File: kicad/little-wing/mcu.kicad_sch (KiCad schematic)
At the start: 30 parts, among them J8 Conn_ARM_SWD_TagConnect_TC203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, SW2 Reset, U1 ${ALTIUM_VALUE}, X1 ${ALTIUM_VALUE}, X2 ${ALTIUM_VALUE}

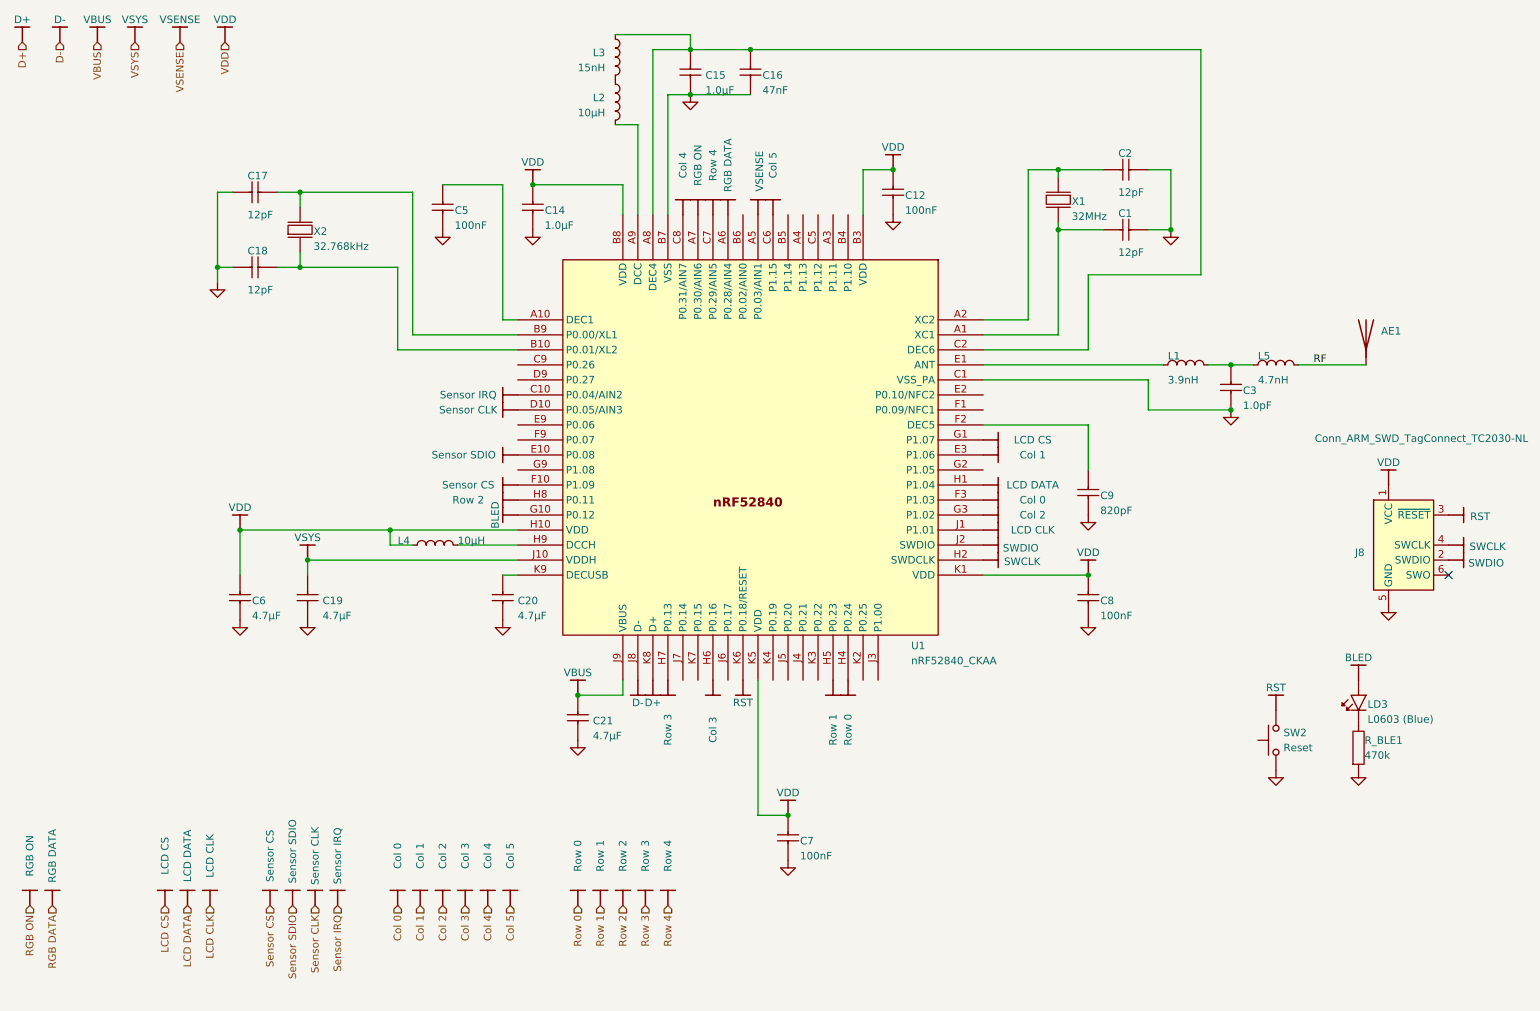
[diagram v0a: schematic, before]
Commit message: Adding the Plan B pins
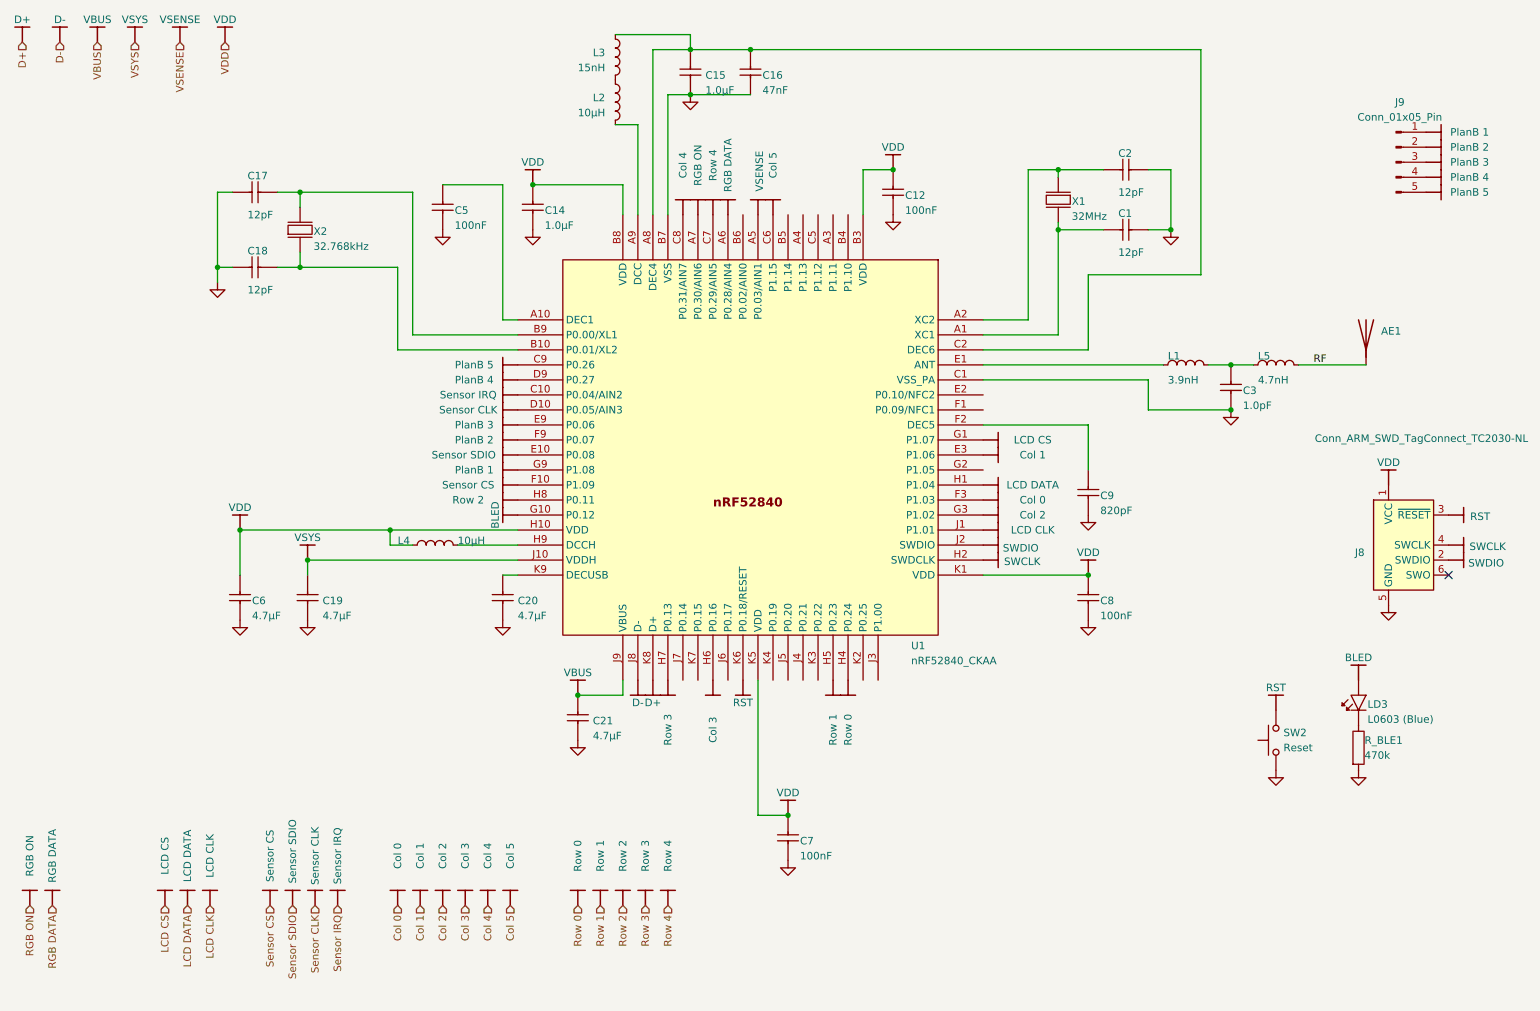
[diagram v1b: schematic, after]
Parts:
- added J9: Conn_01x05_Pin, Connector_JST:JST_SHL_SM05B-SHLS-TF_1x05-1MP_P1.00mm_Horizontal, symbol Connector:Conn_01x05_Pin
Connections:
- net PlanB 5: now reaches U1.C9 (P0.26)
- net PlanB 5: now also J9.5 (Pin_5)
- net PlanB 4: now reaches U1.D9 (P0.27)
- net PlanB 4: now also J9.4 (Pin_4)
- net PlanB 3: now reaches U1.E9 (P0.06)
- net PlanB 3: now also J9.3 (Pin_3)
- net PlanB 2: now reaches U1.F9 (P0.07)
- net PlanB 2: now also J9.2 (Pin_2)
- net PlanB 1: now reaches U1.G9 (P1.08)
- net PlanB 1: now also J9.1 (Pin_1)

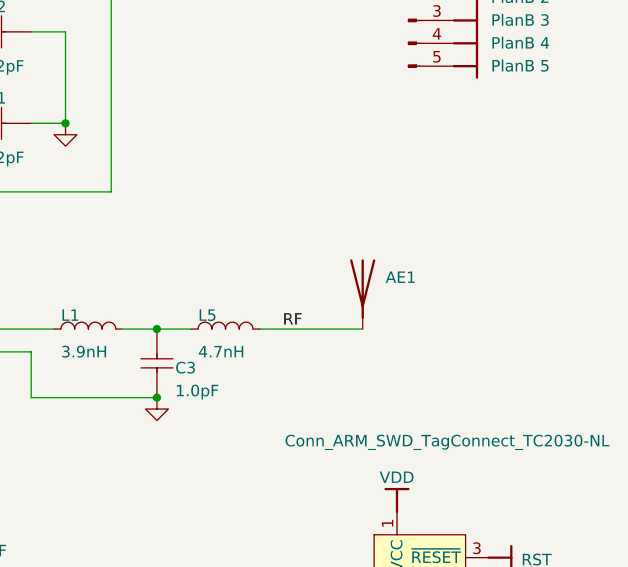
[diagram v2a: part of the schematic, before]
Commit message: Removing the RGB level shifter
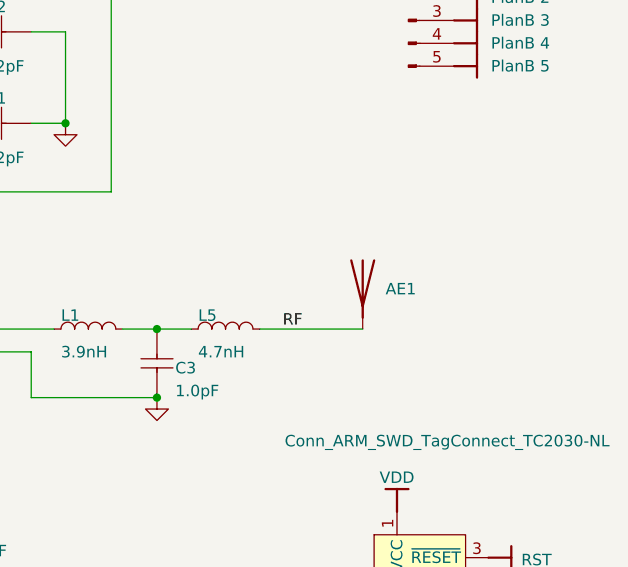
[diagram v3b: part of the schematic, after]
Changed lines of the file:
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@@
 		(fields_autoplaced yes)
 		(property "Reference" "AE1"
-			(at 252.73 75.5649 0)
+			(at 252.73 76.8349 0)
 			(effects
 				(font
